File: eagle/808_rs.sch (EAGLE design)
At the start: 82 parts, among them IC1 TL072P, IC2 TL072P, Q74 MPF102, SW1_A LSP11, SW1_B LSP11, SW1_C LSP11, SW2_A LSP11, SW2_B LSP11, SW2_C LSP11

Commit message: schematic updated
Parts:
- removed C5: 0.1uF, TR808clone:C-EU3.5MM_PITCH
- removed D1: 1N4148DO35-7, TR808clone:1N4148DO35-7
- removed R1: 22K, TR808clone:R-EU_0207/5V
- removed R295: 1K, TR808clone:R-EU_0207/5V
- removed SW1_A, SW1_B, SW1_C, SW2_A, SW2_B, SW2_C: LSP11, solpad:LSP11
- added OUT_NORM: 22-23-2021, con-molex:22-23-2021
- added R238: 1K, TR808clone:R-EU_0207/7
- added SW8: 808_LT_MSS42_SW_4PDT, 808_lt:808_LT_MSS42_SW_4PDT
- OUTPUT: value LSP11 -> AUDIO-JACK; device solpad:LSP11 -> erthenvar:AUDIO-JACK
- Q59, Q61, Q62, Q63: value (none) -> 2N3904; device transistor:BC546-NPN-TO92-CBE -> 808_lt:2N3904
- Q60: value (none) -> 2N3906; device transistor:BC556A-PNP-TO92-EBC -> 808_lt:2N3906
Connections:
- removed net N$345: R319.2, SW1_B.MP
- removed net N$473: R324.1, SW1_C.MP
- removed net RS_CL_OUT: OUTPUT.MP, R295.1
- new net LT_LC_OUT: OUTPUT.TIP, R238.1
- new net N$7: C125.1, SW8G$4.P
- net GND: now also OUTPUT.RING, OUT_NORM-2.S; no longer R1.1
- net N$165: now also SW8G$1.S; no longer SW2_B.MP
- net N$170: now also R238.2; no longer R295.2
- net N$2: now also R319.2, SW8G$4.O; no longer C125.1, SW1_A.MP
- net N$306: now also SW8G$1.O; no longer SW2_C.MP
- net N$338: now also SW8G$1.P; no longer SW2_A.MP
- net N$5: now also OUTPUT.NORM, OUT_NORM-1.S; no longer D1.A, TRIGGER.MP
- net N$6: now also R324.1, SW8G$4.S; no longer C5.1, D1.C, R1.2
- net RS: now also TRIGGER.MP, U$1.GATE; no longer ACCENT.MP
- net TRIG: now also ACCENT.MP, U$1.CV; no longer C5.2
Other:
- moved on the sheet: ACCENT, C118, R309, R313, R319, TRIGGER, U$1

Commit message: 2sk30
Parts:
- removed Q74: MPF102, mes_transistors:MPF102
- added Q1: 2SK30, 808:2SK30
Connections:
- removed net N$170: C153.2, IC2B.OUT, Q74.D, R238.2, R327.1, R330.2, VR16.S
- new net N$8: C153.2, IC2B.OUT, Q1.D, R238.2, R327.1, R330.2, VR16.S
- net N$161: now also Q1.G; no longer Q74.G
- net N$351: now also Q1.S; no longer Q74.S
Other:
- moved on the sheet: C112, C113, Q61, R304, R305, R327

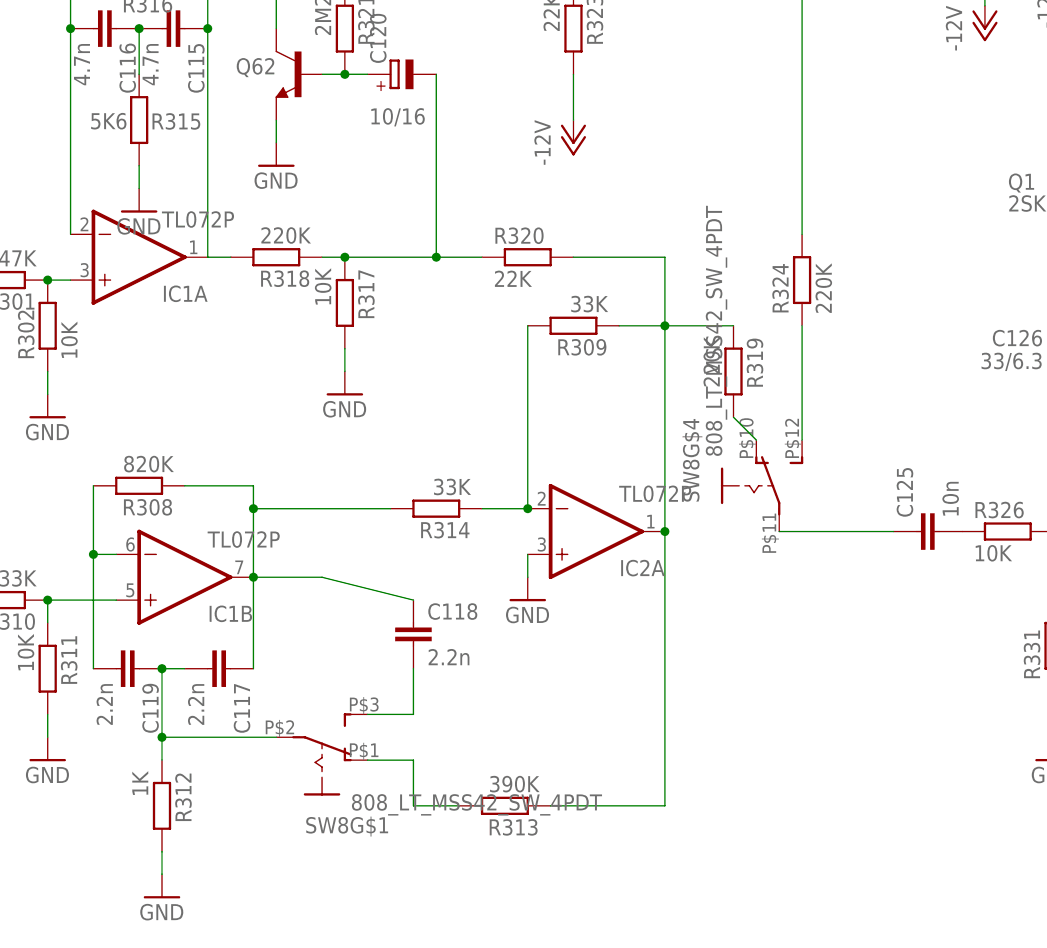
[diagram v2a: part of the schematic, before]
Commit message: restarted layout with care
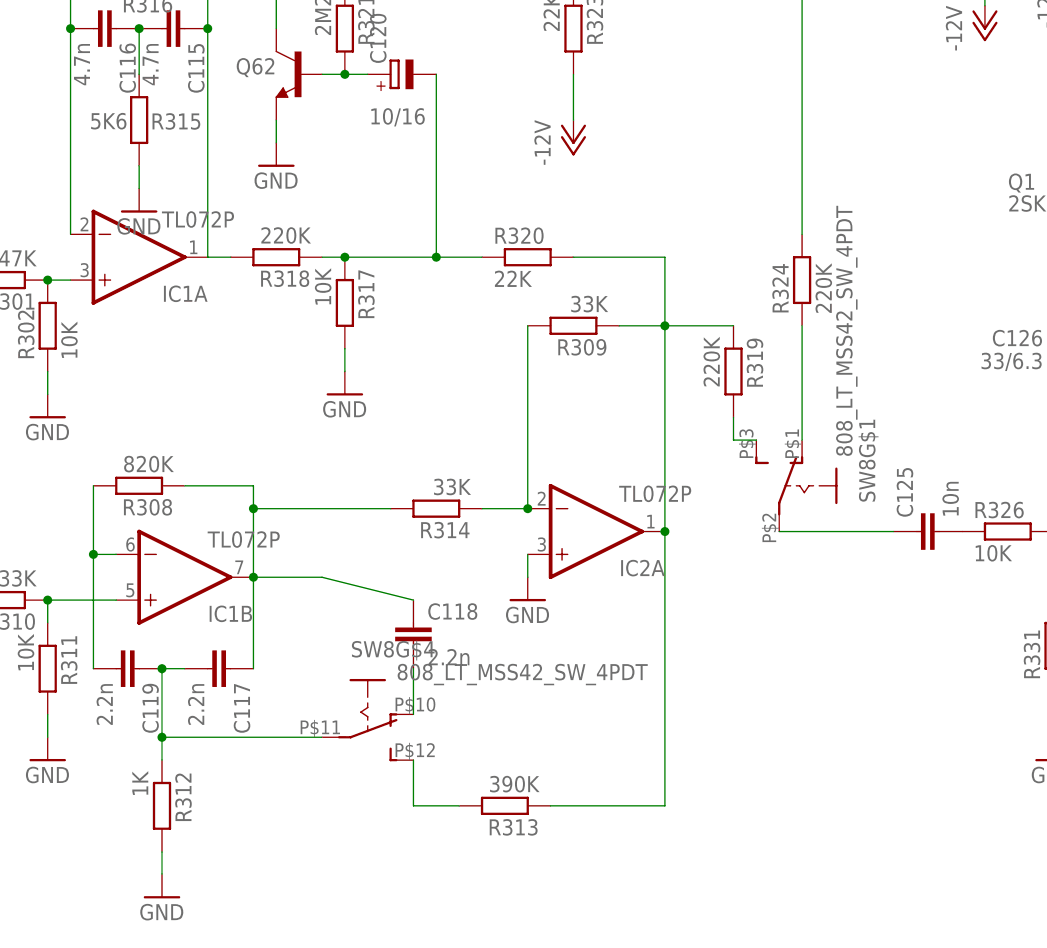
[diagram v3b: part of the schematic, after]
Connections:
- net N$165: now also SW8G$4.O; no longer SW8G$1.S
- net N$2: now also C125.1, SW8G$1.P; no longer R319.2, SW8G$4.O
- net N$306: now also SW8G$4.S; no longer SW8G$1.O
- net N$338: now also SW8G$4.P; no longer SW8G$1.P
- net N$6: now also SW8G$1.O; no longer SW8G$4.S
- net N$7: now also R319.2, SW8G$1.S; no longer C125.1, SW8G$4.P
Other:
- moved on the sheet: SW8G$1, SW8G$4
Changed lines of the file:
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@@
 <instance part="OUT_NORM" gate="-2" x="180.34" y="43.18"/>
 <instance part="V5" gate="1" x="175.26" y="38.1"/>
-<instance part="SW8" gate="G$1" x="60.96" y="-15.24" rot="MR90"/>
-<instance part="SW8" gate="G$4" x="109.22" y="15.24"/>
+<instance part="SW8" gate="G$1" x="114.3" y="15.24" rot="MR0"/>
+<instance part="SW8" gate="G$4" x="66.04" y="-10.16" rot="R270"/>
 <instance part="Q1" gate="G$1" x="152.4" y="45.72" smashed="yes" rot="R270">
 <attribute name="NAME" x="137.16" y="48.133" size="1.778" layer="95"/>
@@
 <wire x1="43.18" y1="-12.7" x2="43.18" y2="-5.08" width="0.1524" layer="91"/>
 <wire x1="45.72" y1="-5.08" x2="43.18" y2="-5.08" width="0.1524" layer="91"/>
-<wire x1="55.88" y1="-12.7" x2="43.18" y2="-12.7" width="0.1524" layer="91"/>
 <junction x="43.18" y="-5.08"/>
-<junction x="43.18" y="-12.7"/>
 <pinref part="R312" gate="G$1" pin="1"/>
 <pinref part="C119" gate="G$1" pin="1"/>
 <pinref part="C117" gate="G$1" pin="2"/>
-<pinref part="SW8" gate="G$1" pin="P"/>
+<pinref part="SW8" gate="G$4" pin="P"/>
+<wire x1="60.96" y1="-12.7" x2="43.18" y2="-12.7" width="0.1524" layer="91"/>
+<junction x="43.18" y="-12.7"/>
 </segment>
 </net>
@@
 <wire x1="71.12" y1="-5.08" x2="71.12" y2="-10.16" width="0.1524" layer="91"/>
 <pinref part="C118" gate="G$1" pin="2"/>
-<pinref part="SW8" gate="G$1" pin="S"/>
-<wire x1="66.04" y1="-10.16" x2="71.12" y2="-10.16" width="0.1524" layer="91"/>
+<pinref part="SW8" gate="G$4" pin="O"/>
 </segment>
 </net>
@@
 <wire x1="71.12" y1="-20.32" x2="76.2" y2="-20.32" width="0.1524" layer="91"/>
 <pinref part="R313" gate="G$1" pin="2"/>
-<pinref part="SW8" gate="G$1" pin="O"/>
-<wire x1="71.12" y1="-15.24" x2="66.04" y2="-15.24" width="0.1524" layer="91"/>
+<pinref part="SW8" gate="G$4" pin="S"/>
 </segment>
 </net>
@@
 <pinref part="OUTPUT" gate="G$1" pin="NORM"/>
 <wire x1="175.26" y1="63.5" x2="180.34" y2="63.5" width="0.1524" layer="91"/>
-</segment>
-</net>
-<net name="N$2" class="0">
-<segment>
-<pinref part="R319" gate="G$1" pin="2"/>
-<wire x1="109.22" y1="20.32" x2="106.68" y2="22.86" width="0.1524" layer="91"/>
-<pinref part="SW8" gate="G$4" pin="O"/>
-</segment>
-</net>
-<net name="N$6" class="0">
-<segment>
-<pinref part="R324" gate="G$1" pin="1"/>
-<wire x1="114.3" y1="33.02" x2="114.3" y2="20.32" width="0.1524" layer="91"/>
-<pinref part="SW8" gate="G$4" pin="S"/>
-</segment>
-</net>
-<net name="N$7" class="0">
-<segment>
-<pinref part="C125" gate="G$1" pin="1"/>
-<wire x1="111.76" y1="10.16" x2="124.46" y2="10.16" width="0.1524" layer="91"/>
-<pinref part="SW8" gate="G$4" pin="P"/>
 </segment>
 </net>
@@
 </segment>
 </net>
+<net name="N$2" class="0">
+<segment>
+<pinref part="SW8" gate="G$1" pin="P"/>
+<pinref part="C125" gate="G$1" pin="1"/>
+<wire x1="111.76" y1="10.16" x2="124.46" y2="10.16" width="0.1524" layer="91"/>
+</segment>
+</net>
+<net name="N$6" class="0">
+<segment>
+<pinref part="SW8" gate="G$1" pin="O"/>
+<pinref part="R324" gate="G$1" pin="1"/>
+<wire x1="114.3" y1="20.32" x2="114.3" y2="33.02" width="0.1524" layer="91"/>
+</segment>
+</net>
+<net name="N$7" class="0">
+<segment>
+<pinref part="SW8" gate="G$1" pin="S"/>
+<pinref part="R319" gate="G$1" pin="2"/>
+<wire x1="109.22" y1="20.32" x2="106.68" y2="20.32" width="0.1524" layer="91"/>
+<wire x1="106.68" y1="20.32" x2="106.68" y2="22.86" width="0.1524" layer="91"/>
+</segment>
+</net>

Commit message: 93pct auto
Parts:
- R305, R306, R310, R311, R316, R323, R324, R325, R326, R331: device TR808clone:R-EU_0207/5V -> TR808clone:R-EU_0207/7
- R313: device TR808clone:R-EU_0207/5V -> TR808clone:R-EU_0309/12
- R318: device TR808clone:R-EU_0207/5V -> TR808clone:R-EU_0207/2V
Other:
- moved on the sheet: C4

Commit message: 95pct auto
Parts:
- C113: device TR808clone:C-EU050-024X044 -> TR808clone:C-EU075-032X103
- C114: device TR808clone:C-EU3.5MM_PITCH -> TR808clone:C-EU050-030X075
- C121: device TR808clone:C-EU3.5MM_PITCH -> TR808clone:C-EU050-025X075
- C4: device TR808clone:C-EU025-025X050 -> TR808clone:C-EU050-024X044
- D61, D63, D64: value 1N4148DO35-7 -> 1N4148DO35-10; device TR808clone:1N4148DO35-7 -> TR808clone:1N4148DO35-10
- R303, R309, R330: device TR808clone:R-EU_0207/5V -> TR808clone:R-EU_0207/2V
- R316: device TR808clone:R-EU_0207/7 -> TR808clone:R-EU_0207/5V
- R321: device TR808clone:R-EU_0207/5V -> TR808clone:R-EU_0207/7
- R326: device TR808clone:R-EU_0207/7 -> TR808clone:R-EU_0309/10
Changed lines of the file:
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@@
 <part name="Q59" library="808_lt" deviceset="2N3904" device=""/>
 <part name="Q60" library="808_lt" deviceset="2N3906" device=""/>
-<part name="R303" library="TR808clone" deviceset="R-EU_" device="0207/5V" value="10K"/>
+<part name="R303" library="TR808clone" deviceset="R-EU_" device="0207/2V" value="10K"/>
 <part name="R297" library="TR808clone" deviceset="R-EU_" device="0207/5V" value="22K"/>
 <part name="R299" library="TR808clone" deviceset="R-EU_" device="0207/5V" value="4K7"/>
@@
 <part name="V200" library="supply1" deviceset="GND" device=""/>
 <part name="V201" library="supply1" deviceset="GND" device=""/>
-<part name="D61" library="TR808clone" deviceset="1N4148" device="DO35-7"/>
+<part name="D61" library="TR808clone" deviceset="1N4148" device="DO35-10" value="1N4148DO35-10"/>
 <part name="V202" library="supply1" deviceset="GND" device=""/>
 <part name="R107" library="TR808clone" deviceset="R-EU_" device="0207/5V" value="1K"/>
 <part name="V203" library="supply1" deviceset="GND" device=""/>
 <part name="R108" library="TR808clone" deviceset="R-EU_" device="0207/5V" value="10K"/>
-<part name="D63" library="TR808clone" deviceset="1N4148" device="DO35-7"/>
-<part name="C121" library="TR808clone" deviceset="C-EU" device="3.5MM_PITCH" value="4.7n"/>
+<part name="D63" library="TR808clone" deviceset="1N4148" device="DO35-10" value="1N4148DO35-10"/>
+<part name="C121" library="TR808clone" deviceset="C-EU" device="050-025X075" value="4.7n"/>
 <part name="C122" library="TR808clone" deviceset="C-EU" device="3.5MM_PITCH" value="4.7n"/>
 <part name="R325" library="TR808clone" deviceset="R-EU_" device="0207/7" value="330K"/>
@@
 <part name="V208" library="supply1" deviceset="GND" device=""/>
 <part name="R301" library="TR808clone" deviceset="R-EU_" device="0207/5V" value="47K"/>
-<part name="C114" library="TR808clone" deviceset="C-EU" device="3.5MM_PITCH" value="1n"/>
+<part name="C114" library="TR808clone" deviceset="C-EU" device="050-030X075" value="1n"/>
 <part name="R306" library="TR808clone" deviceset="R-EU_" device="0207/7" value="22K"/>
-<part name="D64" library="TR808clone" deviceset="1N4148" device="DO35-7"/>
+<part name="D64" library="TR808clone" deviceset="1N4148" device="DO35-10" value="1N4148DO35-10"/>
 <part name="R310" library="TR808clone" deviceset="R-EU_" device="0207/7" value="33K"/>
 <part name="R311" library="TR808clone" deviceset="R-EU_" device="0207/7" value="10K"/>
@@
 <part name="R313" library="TR808clone" deviceset="R-EU_" device="0309/12" value="390K"/>
 <part name="V212" library="supply1" deviceset="GND" device=""/>
-<part name="R309" library="TR808clone" deviceset="R-EU_" device="0207/5V" value="33K"/>
+<part name="R309" library="TR808clone" deviceset="R-EU_" device="0207/2V" value="33K"/>
 <part name="R319" library="TR808clone" deviceset="R-EU_" device="0207/5V" value="220K"/>
 <part name="C125" library="TR808clone" deviceset="C-EU" device="3.5MM_PITCH" value="10n"/>
-<part name="R326" library="TR808clone" deviceset="R-EU_" device="0207/7" value="10K"/>
+<part name="R326" library="TR808clone" deviceset="R-EU_" device="0309/10" value="10K"/>
 <part name="R331" library="TR808clone" deviceset="R-EU_" device="0207/7" value="47K"/>
 <part name="V213" library="supply1" deviceset="GND" device=""/>
 <part name="C153" library="TR808clone" deviceset="C-EU" device="025-025X050" value="22p"/>
-<part name="R330" library="TR808clone" deviceset="R-EU_" device="0207/5V" value="470K"/>
+<part name="R330" library="TR808clone" deviceset="R-EU_" device="0207/2V" value="470K"/>
 <part name="C126" library="TR808clone" deviceset="CPOL-EU" device="E2.5-5" value="33/6.3"/>
 <part name="C116" library="TR808clone" deviceset="C-EU" device="3.5MM_PITCH" value="4.7n"/>
@@
 <part name="R315" library="TR808clone" deviceset="R-EU_" device="0207/5V" value="5K6"/>
 <part name="V214" library="supply1" deviceset="GND" device=""/>
-<part name="R316" library="TR808clone" deviceset="R-EU_" device="0207/7" value="1M"/>
+<part name="R316" library="TR808clone" deviceset="R-EU_" device="0207/5V" value="1M"/>
 <part name="R318" library="TR808clone" deviceset="R-EU_" device="0207/2V" value="220K"/>
 <part name="R317" library="TR808clone" deviceset="R-EU_" device="0207/5V" value="10K"/>
 <part name="Q62" library="808_lt" deviceset="2N3904" device=""/>
 <part name="V215" library="supply1" deviceset="GND" device=""/>
-<part name="R321" library="TR808clone" deviceset="R-EU_" device="0207/5V" value="2M2"/>
+<part name="R321" library="TR808clone" deviceset="R-EU_" device="0207/7" value="2M2"/>
 <part name="C120" library="TR808clone" deviceset="CPOL-EU" device="E2.5-5" value="10/16"/>
 <part name="V217" library="supply1" deviceset="GND" device=""/>
@@
 <part name="Q61" library="808_lt" deviceset="2N3904" device=""/>
 <part name="C112" library="TR808clone" deviceset="C-EU" device="050-024X044" value="22n"/>
-<part name="C113" library="TR808clone" deviceset="C-EU" device="050-024X044" value="47n"/>
+<part name="C113" library="TR808clone" deviceset="C-EU" device="075-032X103" value="47n"/>
 <part name="R304" library="TR808clone" deviceset="R-EU_" device="0207/5V" value="47K"/>
 <part name="R305" library="TR808clone" deviceset="R-EU_" device="0207/7" value="1M"/>
@@
 <part name="C2" library="TR808clone" deviceset="C-EU" device="025-025X050" value="22p"/>
 <part name="C3" library="TR808clone" deviceset="C-EU" device="025-025X050" value="22p"/>
-<part name="C4" library="TR808clone" deviceset="C-EU" device="025-025X050" value="22p"/>
+<part name="C4" library="TR808clone" deviceset="C-EU" device="050-024X044" value="22p"/>
 <part name="TRIGGER" library="solpad" deviceset="LSP11" device=""/>
 <part name="SW8" library="808_lt" deviceset="808_LT_MSS42_SW_4PDT" device=""/>

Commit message: 94pct auto
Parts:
- C118: device TR808clone:C-EU3.5MM_PITCH -> TR808clone:C-EU050-024X044
- C122: device TR808clone:C-EU3.5MM_PITCH -> TR808clone:C-EU050-030X075
- R318: device TR808clone:R-EU_0207/2V -> TR808clone:R-EU_0207/5V
- R320, R322: device TR808clone:R-EU_0207/5V -> TR808clone:R-EU_0207/7
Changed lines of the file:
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@@
 <part name="D63" library="TR808clone" deviceset="1N4148" device="DO35-10" value="1N4148DO35-10"/>
 <part name="C121" library="TR808clone" deviceset="C-EU" device="050-025X075" value="4.7n"/>
-<part name="C122" library="TR808clone" deviceset="C-EU" device="3.5MM_PITCH" value="4.7n"/>
+<part name="C122" library="TR808clone" deviceset="C-EU" device="050-030X075" value="4.7n"/>
 <part name="R325" library="TR808clone" deviceset="R-EU_" device="0207/7" value="330K"/>
 <part name="Q63" library="808_lt" deviceset="2N3904" device=""/>
 <part name="R323" library="TR808clone" deviceset="R-EU_" device="0207/7" value="22K"/>
-<part name="R322" library="TR808clone" deviceset="R-EU_" device="0207/5V" value="10K"/>
+<part name="R322" library="TR808clone" deviceset="R-EU_" device="0207/7" value="10K"/>
 <part name="V204" library="supply1" deviceset="GND" device=""/>
 <part name="C111" library="TR808clone" deviceset="C-EU" device="3.5MM_PITCH" value="10n"/>
@@
 <part name="C119" library="TR808clone" deviceset="C-EU" device="3.5MM_PITCH" value="2.2n"/>
 <part name="C117" library="TR808clone" deviceset="C-EU" device="3.5MM_PITCH" value="2.2n"/>
-<part name="C118" library="TR808clone" deviceset="C-EU" device="3.5MM_PITCH" value="2.2n"/>
+<part name="C118" library="TR808clone" deviceset="C-EU" device="050-024X044" value="2.2n"/>
 <part name="R312" library="TR808clone" deviceset="R-EU_" device="0207/5V" value="1K"/>
 <part name="V211" library="supply1" deviceset="GND" device=""/>
@@
 <part name="V214" library="supply1" deviceset="GND" device=""/>
 <part name="R316" library="TR808clone" deviceset="R-EU_" device="0207/5V" value="1M"/>
-<part name="R318" library="TR808clone" deviceset="R-EU_" device="0207/2V" value="220K"/>
+<part name="R318" library="TR808clone" deviceset="R-EU_" device="0207/5V" value="220K"/>
 <part name="R317" library="TR808clone" deviceset="R-EU_" device="0207/5V" value="10K"/>
 <part name="Q62" library="808_lt" deviceset="2N3904" device=""/>
@@
 <part name="VR16" library="pot" deviceset="3RP/1610N" device="" value="100KA"/>
 <part name="R324" library="TR808clone" deviceset="R-EU_" device="0207/7" value="220K"/>
-<part name="R320" library="TR808clone" deviceset="R-EU_" device="0207/5V" value="22K"/>
+<part name="R320" library="TR808clone" deviceset="R-EU_" device="0207/7" value="22K"/>
 <part name="Q61" library="808_lt" deviceset="2N3904" device=""/>
 <part name="C112" library="TR808clone" deviceset="C-EU" device="050-024X044" value="22n"/>
